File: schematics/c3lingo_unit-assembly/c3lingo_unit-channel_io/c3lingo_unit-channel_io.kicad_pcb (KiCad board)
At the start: 2 copper layers, 75 x 45 mm, 40 parts, among them J601 Mic X In, J602 Headphone X, J603 Interconnect, J604 PowerSupply, U601 NE5534, U602 TPA6111A2

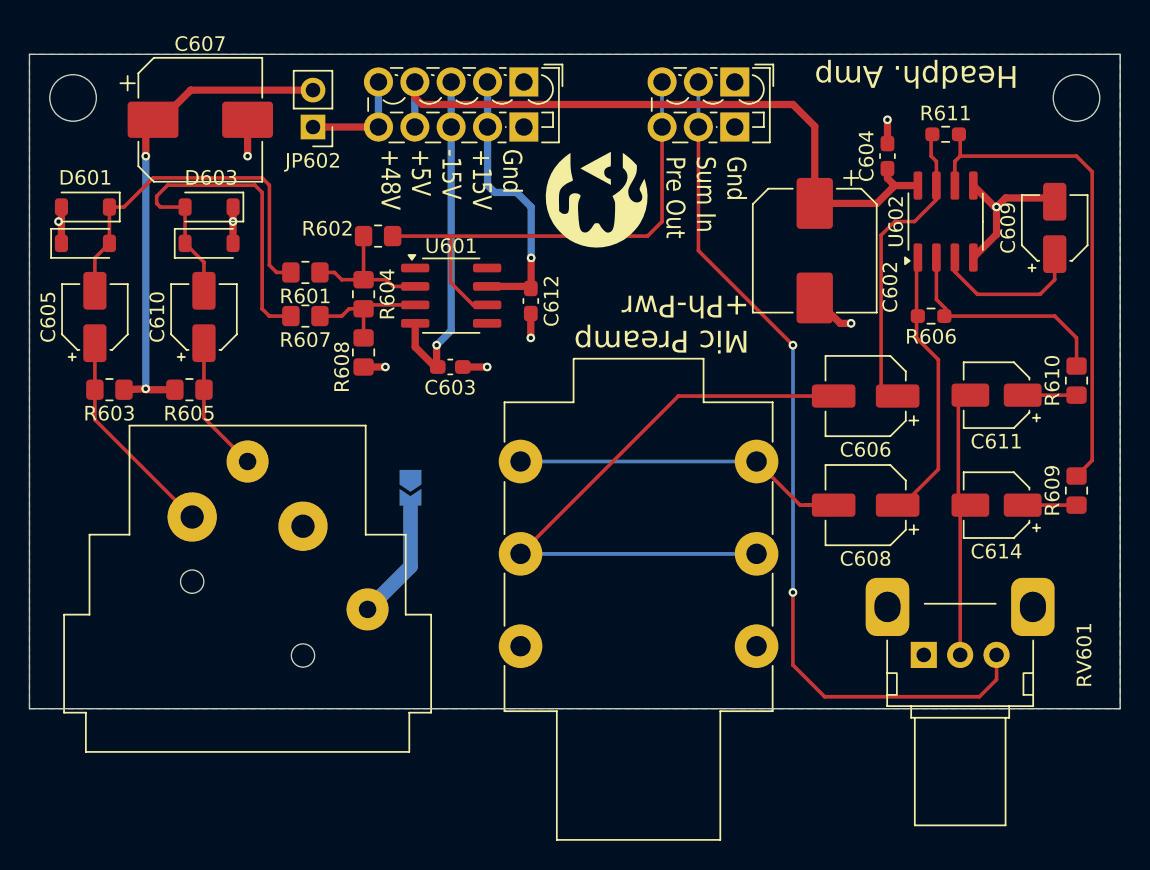
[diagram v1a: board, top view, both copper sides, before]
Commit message: Change inter-PCB connections to IDC connectors
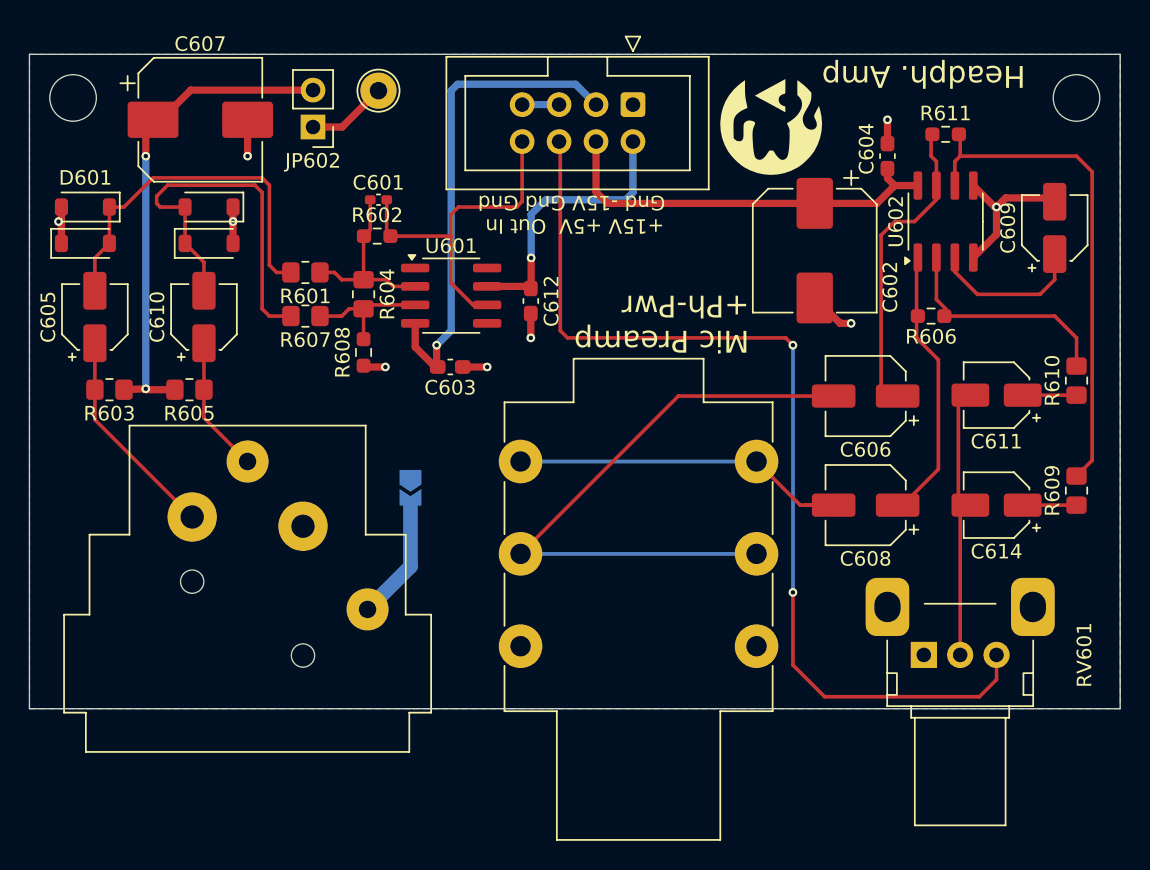
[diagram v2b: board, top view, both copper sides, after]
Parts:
- removed J604: PowerSupply, TerminalBlock_Phoenix:TerminalBlock_Phoenix_PTSM-0,5-5-2.5-V-THR_1x05_P2.50mm_Vertical
- added C601: 220p, Capacitor_SMD:C_0402_1005Metric_Pad0.74x0.62mm_HandSolder, F.Cu at (74.0, 165.0)
- added TP601: Phantom Power, TestPoint:TestPoint_THTPad_D2.5mm_Drill1.2mm, F.Cu at (74.0, 157.5)
- J603: footprint TerminalBlock_Phoenix:TerminalBlock_Phoenix_PTSM-0,5-3-2.5-V-THR_1x03_P2.50mm_Vertical -> Connector_IDC:IDC-Header_2x04_P2.54mm_Vertical
- R602, R608: value 68K 1% -> 39K 1%; footprint Resistor_SMD:R_0805_2012Metric_Pad1.20x1.40mm_HandSolder -> Resistor_SMD:R_0603_1608Metric_Pad0.98x0.95mm_HandSolder
- moved G*** 13.0 mm to (101.0, 160.0)
- moved J603 7.17 mm to (91.5, 158.5), turned to -90 degrees
- moved G*** 0.50 mm to (87.5, 175.5)
- moved R602 0.06 mm to (73.9, 167.5)
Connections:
- J603 pad 2: /Headphone -> +15V
- J603 pad 3: /MicPre -> -15V
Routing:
- net +5V: track 46.8 -> 27.8 mm
- net /MicPre: track 34.9 -> 23.8 mm
- net -15V: track 23.6 -> 33.7 mm
- net /Headphone: track 59.9 -> 68.6 mm
- net Net-(U601--): track 9.95 -> 12.6 mm
- net GND: track 27.6 -> 30.2 mm
- net Net-(JP602-A): track 7.60 -> 5.54 mm
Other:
- board text added: "+15V +5V Out In Gnd -15V Gnd Gnd"
- board text added: "c3lingo Interpreter Unit Channel I/O v0.4.0 2025-08-26"
- board text removed: "Gnd +15V -15V +5V +48V"
- board text removed: "Gnd Sum In Pre Out"
- board text removed: "c3lingo Interpreter Unit Channel I/O v0.3.3 2024-09-08"

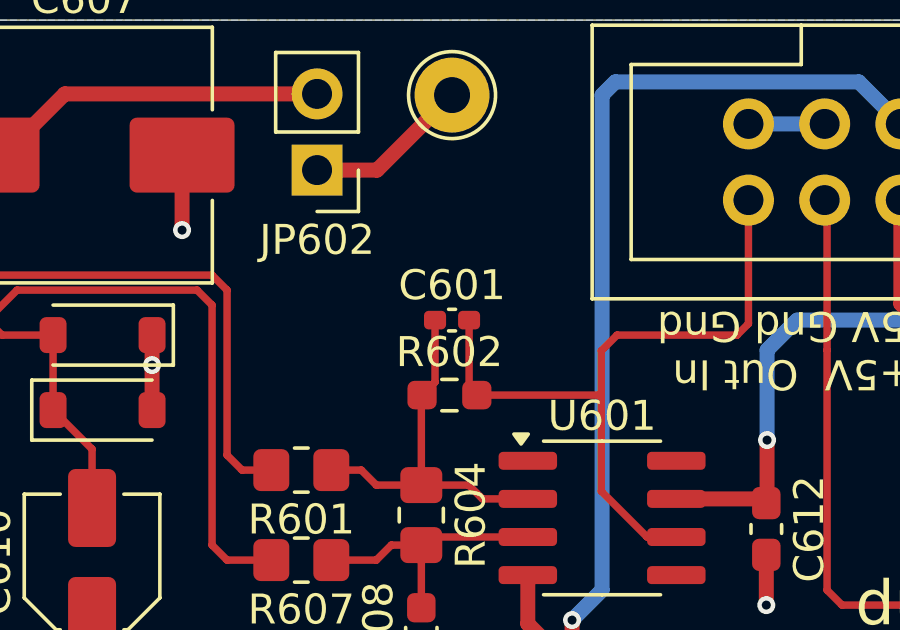
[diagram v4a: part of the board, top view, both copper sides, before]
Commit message: Channel I/O: Fix value of C601
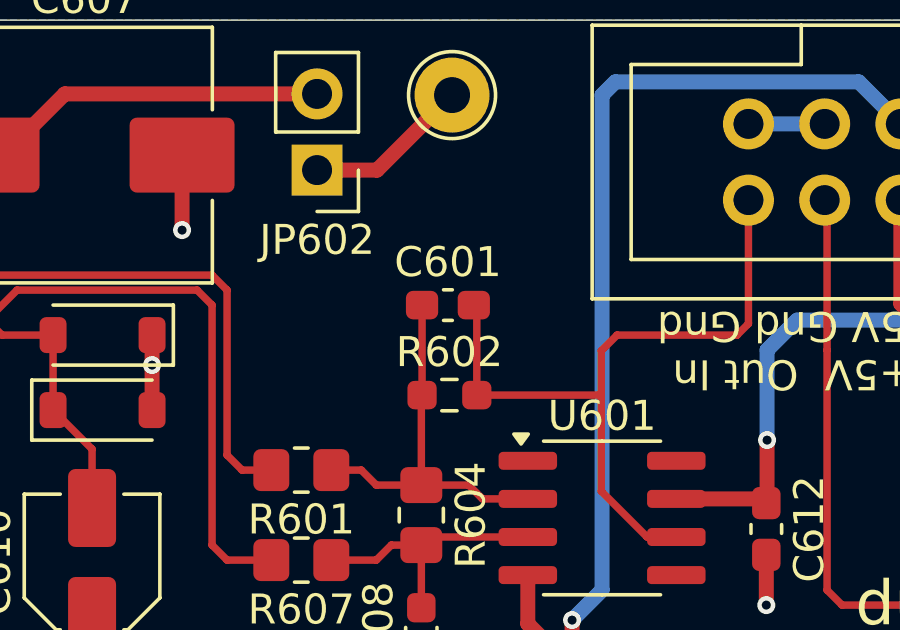
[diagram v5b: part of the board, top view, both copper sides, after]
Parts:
- C601: value 220p -> 330p; footprint Capacitor_SMD:C_0402_1005Metric_Pad0.74x0.62mm_HandSolder -> Capacitor_SMD:C_0603_1608Metric_Pad1.08x0.95mm_HandSolder
- moved C601 0.52 mm to (73.9, 164.5)
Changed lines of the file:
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@@
 	(title_block
 		(title "c3lingo interpeter unit -- channel I/O")
-		(date "2025-08-26")
-		(rev "v0.4.0")
+		(date "2025-08-31")
+		(rev "v0.4.1")
 		(company "Jannik Beyerstedt (jtbx)")
 		(comment 1 "Prototype 3")
@@
 		(embedded_fonts no)
 	)
-	(footprint "Capacitor_SMD:C_0402_1005Metric_Pad0.74x0.62mm_HandSolder"
+	(footprint "Capacitor_SMD:C_0603_1608Metric_Pad1.08x0.95mm_HandSolder"
 		(layer "F.Cu")
-		(at 74 165)
-		(descr "Capacitor SMD 0402 (1005 Metric), square (rectangular) end terminal, IPC-7351 nominal with elongated pad for handsoldering. (Body size source: IPC-SM-782 page 76, https://www.pcb-3d.com/wordpress/wp-content/uploads/ipc-sm-782a_amendment_1_and_2.pdf), generated with kicad-footprint-generator")
+		(at 73.8625 164.5)
+		(descr "Capacitor SMD 0603 (1608 Metric), square (rectangular) end terminal, IPC-7351 nominal with elongated pad for handsoldering. (Body size source: IPC-SM-782 page 76, https://www.pcb-3d.com/wordpress/wp-content/uploads/ipc-sm-782a_amendment_1_and_2.pdf), generated with kicad-footprint-generator")
 		(tags "capacitor handsolder")
 		(property "Reference" "C601"
-			(at 0 -1.16 0)
+			(at 0 -1.43 0)
 			(layer "F.SilkS")
 			(effects
@@
 			)
 		)
-		(property "Value" "220p"
-			(at 0 1.16 0)
+		(property "Value" "330p"
+			(at 0 1.43 0)
 			(layer "F.Fab")
 			(effects
@@
 			)
 		)
-		(property "LCSC Part #" "C107001"
+		(property "LCSC Part #" "C1664"
 			(at 0 0 0)
 			(unlocked yes)
@@
 		(attr smd)
 		(fp_line
-			(start -0.115835 -0.36)
-			(end 0.115835 -0.36)
+			(start -0.146267 -0.51)
+			(end 0.146267 -0.51)
 			(stroke
 				(width 0.12)
@@
 		)
 		(fp_line
-			(start -0.115835 0.36)
-			(end 0.115835 0.36)
+			(start -0.146267 0.51)
+			(end 0.146267 0.51)
 			(stroke
 				(width 0.12)
@@
 		)
 		(fp_line
-			(start -1.09 -0.46)
-			(end 1.09 -0.46)
+			(start -1.65 -0.73)
+			(end 1.65 -0.73)
 			(stroke
 				(width 0.05)
@@
 		)
 		(fp_line
-			(start -1.09 0.46)
-			(end -1.09 -0.46)
+			(start -1.65 0.73)
+			(end -1.65 -0.73)
 			(stroke
 				(width 0.05)
@@
 		)
 		(fp_line
-			(start 1.09 -0.46)
-			(end 1.09 0.46)
+			(start 1.65 -0.73)
+			(end 1.65 0.73)
 			(stroke
 				(width 0.05)
@@
 		)
 		(fp_line
-			(start 1.09 0.46)
-			(end -1.09 0.46)
+			(start 1.65 0.73)
+			(end -1.65 0.73)
 			(stroke
 				(width 0.05)
@@
 		)
 		(fp_line
-			(start -0.5 -0.25)
-			(end 0.5 -0.25)
+			(start -0.8 -0.4)
+			(end 0.8 -0.4)
 			(stroke
 				(width 0.1)
@@
 		)
 		(fp_line
-			(start -0.5 0.25)
-			(end -0.5 -0.25)
+			(start -0.8 0.4)
+			(end -0.8 -0.4)
 			(stroke
 				(width 0.1)
@@
 		)
 		(fp_line
-			(start 0.5 -0.25)
-			(end 0.5 0.25)
+			(start 0.8 -0.4)
+			(end 0.8 0.4)
 			(stroke
 				(width 0.1)
@@
 		)
 		(fp_line
-			(start 0.5 0.25)
-			(end -0.5 0.25)
+			(start 0.8 0.4)
+			(end -0.8 0.4)
 			(stroke
 				(width 0.1)
@@
 			(layer "F.Fab")
 		)
-		(fp_text user "${REFERENCE}"
-			(at 0 0 0)
-			(layer "F.Fab")
-			(effects
-				(font
-					(size 0.25 0.25)
-					(thickness 0.04)
-				)
-			)
-		)
 		(pad "1" smd roundrect
-			(at -0.5675 0)
-			(size 0.735 0.62)
+			(at -0.8625 0)
+			(size 1.075 0.95)
 			(layers "F.Cu" "F.Mask" "F.Paste")
 			(roundrect_rratio 0.25)
@@
 		)
 		(pad "2" smd roundrect
-			(at 0.5675 0)
-			(size 0.735 0.62)
+			(at 0.8625 0)
+			(size 1.075 0.95)
 			(layers "F.Cu" "F.Mask" "F.Paste")
 			(roundrect_rratio 0.25)
@@
 		)
 		(embedded_fonts no)
-		(model "${KICAD9_3DMODEL_DIR}/Capacitor_SMD.3dshapes/C_0402_1005Metric.step"
+		(model "${KICAD9_3DMODEL_DIR}/Capacitor_SMD.3dshapes/C_0603_1608Metric.step"
 			(offset
 				(xyz 0 0 0)
@@
 	)
 	(segment
-		(start 71.475 170.5)
-		(end 70.975 170)
-		(width 0.25)
-		(layer "F.Cu")
-		(net 16)
-	)
-	(segment
-		(start 75.015 170.96)
-		(end 74.555 170.5)
+		(start 73 167.5)
+		(end 73 164.5)
 		(width 0.25)
 		(layer "F.Cu")
@@
 	)
 	(segment
-		(start 73.4325 165)
-		(end 73.4325 167.0675)
+		(start 71.475 170.5)
+		(end 70.975 170)
 		(width 0.25)
 		(layer "F.Cu")
@@
 	)
 	(segment
-		(start 73.4325 167.0675)
-		(end 73 167.5)
+		(start 75.015 170.96)
+		(end 74.555 170.5)
 		(width 0.25)
 		(layer "F.Cu")
@@
 	)
 	(segment
-		(start 74.5675 165)
-		(end 74.5675 167.2425)
+		(start 74.825 164.6)
+		(end 74.725 164.5)
 		(width 0.25)
 		(layer "F.Cu")
@@
 	)
 	(segment
-		(start 74.5675 167.2425)
-		(end 74.825 167.5)
+		(start 79.5 165.5)
+		(end 78.975 166.025)
 		(width 0.25)
 		(layer "F.Cu")
@@
 	)
 	(segment
-		(start 79.5 165.5)
-		(end 78.975 166.025)
+		(start 81.475 172.23)
+		(end 80.500001 172.23)
 		(width 0.25)
 		(layer "F.Cu")
@@
 	)
 	(segment
-		(start 81.475 172.23)
-		(end 80.500001 172.23)
+		(start 74.825 167.5)
+		(end 74.825 164.6)
 		(width 0.25)
 		(layer "F.Cu")

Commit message: WIP: Add some artwork to the PCBs
TODO: OSHW
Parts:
- added G***: LOGO, c3lingo_unit-footprints:chaosknoten-10mm, B.Cu at (104.5, 174.5)
- added G***: LOGO, c3lingo_unit-footprints:antifa-10mm, B.Cu at (71.0, 176.0)
